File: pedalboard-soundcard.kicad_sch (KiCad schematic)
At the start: 21 parts, among them J1 RPi_GPIO, U1 AT24CS01-STUM, U2 NCP163, U3 NCP163, U5 NCP163

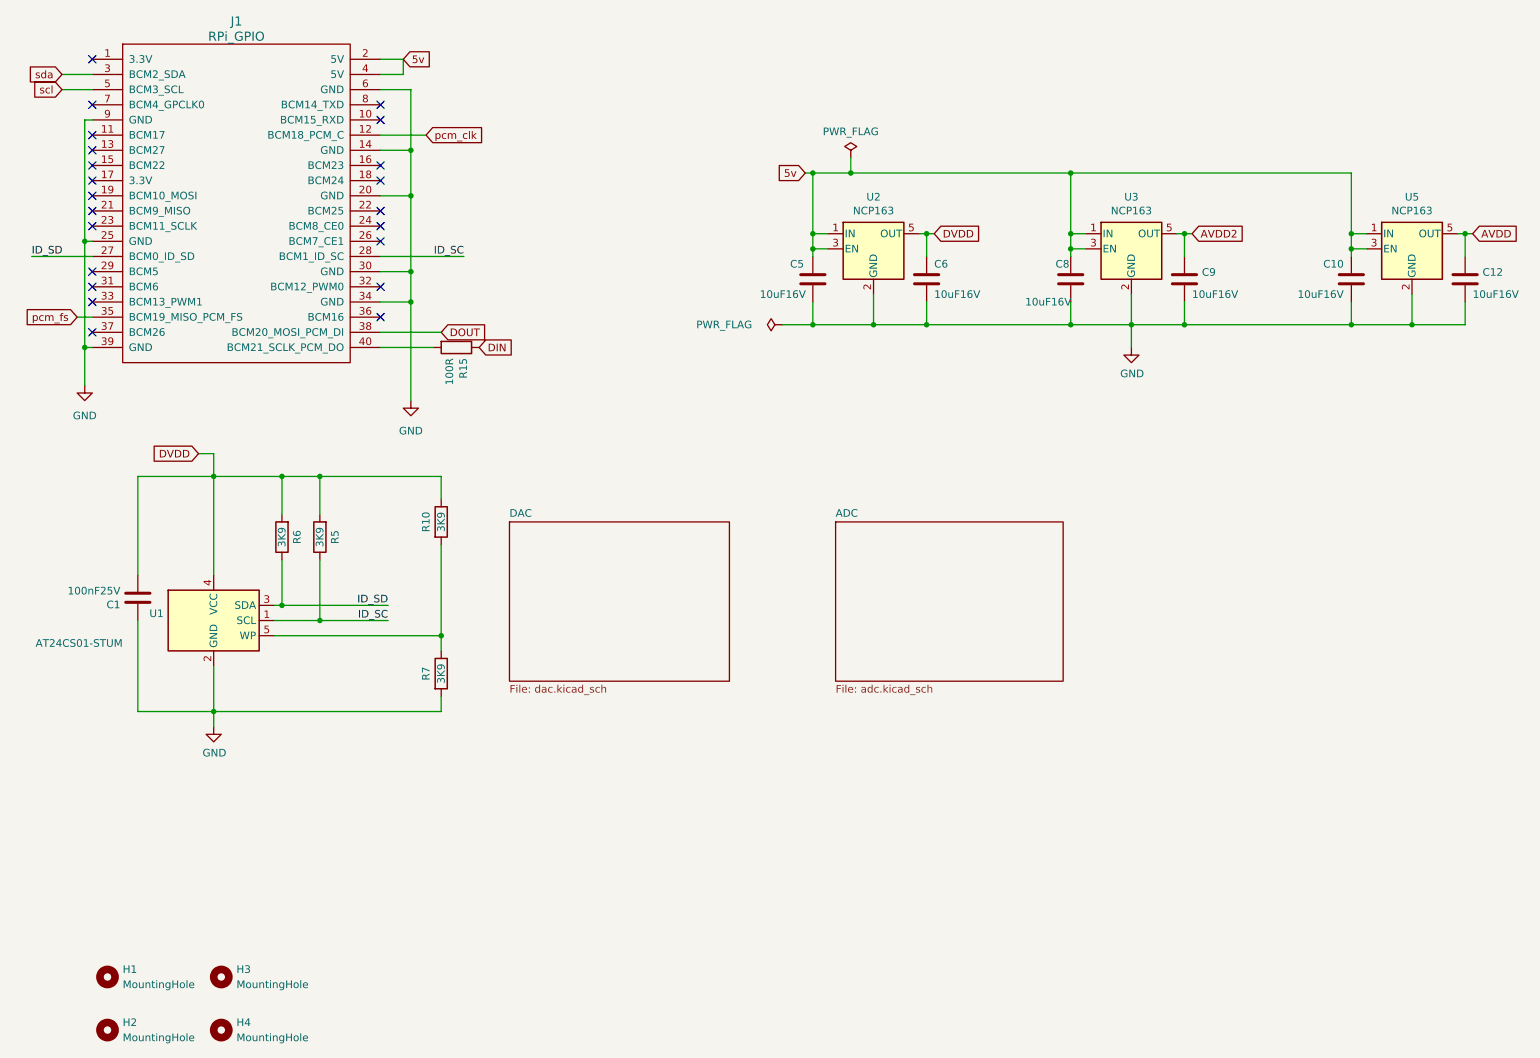
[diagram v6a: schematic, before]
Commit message: Replace 5v global label with +5V power
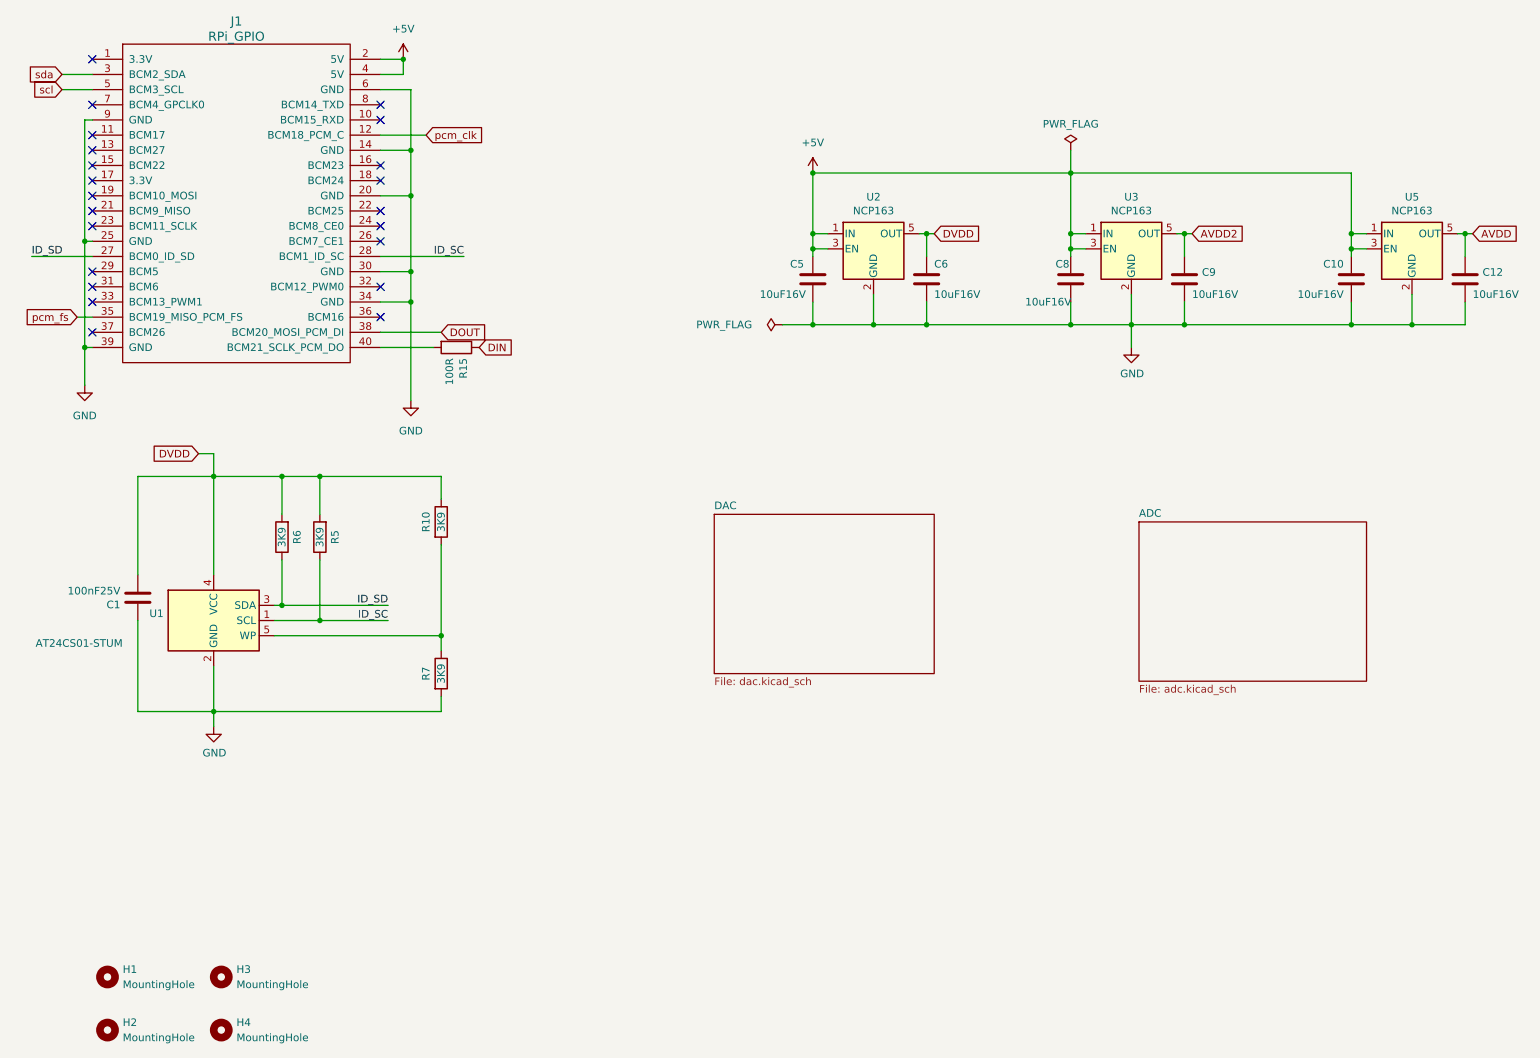
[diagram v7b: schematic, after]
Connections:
- net 5v renamed +5V
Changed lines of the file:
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@@
   (junction (at 44.45 96.52) (diameter 0) (color 0 0 0 0)
   )
+  (junction (at 144.78 45.72) (diameter 0) (color 0 0 0 0)
+  )
   (junction (at 234.95 71.12) (diameter 0) (color 0 0 0 0)
   )
   (junction (at 163.83 71.12) (diameter 0) (color 0 0 0 0)
   )
-  (junction (at 151.13 45.72) (diameter 0) (color 0 0 0 0)
-  )
   (junction (at 245.11 71.12) (diameter 0) (color 0 0 0 0)
   )
@@
   (junction (at 144.78 55.88) (diameter 0) (color 0 0 0 0)
   )
+  (junction (at 76.2 26.67) (diameter 0) (color 0 0 0 0)
+  )
   (junction (at 77.47 62.23) (diameter 0) (color 0 0 0 0)
   )
@@
   )
   (junction (at 77.47 49.53) (diameter 0) (color 0 0 0 0)
-  )
-  (junction (at 144.78 45.72) (diameter 0) (color 0 0 0 0)
   )
   (junction (at 77.47 41.91) (diameter 0) (color 0 0 0 0)
@@
     (stroke (width 0) (type default))
   )
-  (wire (pts (xy 143.51 45.72) (xy 144.78 45.72))
-    (stroke (width 0) (type default))
-  )
   (wire (pts (xy 207.01 55.88) (xy 208.28 55.88))
     (stroke (width 0) (type default))
@@
     (stroke (width 0) (type default))
   )
-  (wire (pts (xy 151.13 43.18) (xy 151.13 45.72))
+  (wire (pts (xy 187.96 41.91) (xy 187.96 45.72))
     (stroke (width 0) (type default))
   )
@@
     (stroke (width 0) (type default))
   )
-  (wire (pts (xy 144.78 45.72) (xy 151.13 45.72))
-    (stroke (width 0) (type default))
-  )
   (wire (pts (xy 31.75 96.52) (xy 31.75 113.03))
     (stroke (width 0) (type default))
@@
     (stroke (width 0) (type default))
   )
-  (wire (pts (xy 151.13 45.72) (xy 187.96 45.72))
+  (wire (pts (xy 144.78 45.72) (xy 187.96 45.72))
     (stroke (width 0) (type default))
   )
@@
     (effects (font (size 1.27 1.27)) (justify right))
     (property "Intersheetrefs" "${INTERSHEET_REFS}" (at 19.05 29.21 0)
-      (effects (font (size 1.27 1.27)) hide)
-    )
-  )
-  (global_label "5v" (shape input) (at 143.51 45.72 180)
-    (effects (font (size 1.27 1.27)) (justify right))
-    (property "Intersheetrefs" "${INTERSHEET_REFS}" (at 143.51 45.72 0)
       (effects (font (size 1.27 1.27)) hide)
     )
@@
     )
   )
-  (global_label "5v" (shape input) (at 76.2 26.67 0) (fields_autoplaced)
-    (effects (font (size 1.27 1.27)) (justify left))
-    (property "Intersheetrefs" "${INTERSHEET_REFS}" (at 80.7081 26.67 0)
-      (effects (font (size 1.27 1.27)) (justify left) hide)
-    )
-  )
   (global_label "DVDD" (shape input) (at 41.91 92.71 180)
     (effects (font (size 1.27 1.27)) (justify right))
@@
     )
   )
+  (symbol (lib_id "power:+5V") (at 76.2 26.67 0) (unit 1)
+    (in_bom yes) (on_board yes) (dnp no) (fields_autoplaced)
+    (property "Reference" "#PWR018" (at 76.2 30.48 0)
+      (effects (font (size 1.27 1.27)) hide)
+    )
+    (property "Value" "+5V" (at 76.2 21.59 0)
+      (effects (font (size 1.27 1.27)))
+    )
+    (property "Footprint" "" (at 76.2 26.67 0)
+      (effects (font (size 1.27 1.27)) hide)
+    )
+    (property "Datasheet" "" (at 76.2 26.67 0)
+      (effects (font (size 1.27 1.27)) hide)
+    )
+    (pin "1")
+    (instances
+      (project "pedalboard-soundcard"
+        (path "/257597c6-fbef-4478-b0f4-968f2d6f1866"
+          (reference "#PWR018") (unit 1)
+        )
+      )
+    )
+  )
+  (symbol (lib_id "power:+5V") (at 144.78 45.72 0) (unit 1)
+    (in_bom yes) (on_board yes) (dnp no) (fields_autoplaced)
+    (property "Reference" "#PWR019" (at 144.78 49.53 0)
+      (effects (font (size 1.27 1.27)) hide)
+    )
+    (property "Value" "+5V" (at 144.78 40.64 0)
+      (effects (font (size 1.27 1.27)))
+    )
+    (property "Footprint" "" (at 144.78 45.72 0)
+      (effects (font (size 1.27 1.27)) hide)
+    )
+    (property "Datasheet" "" (at 144.78 45.72 0)
+      (effects (font (size 1.27 1.27)) hide)
+    )
+    (pin "1")
+    (instances
+      (project "pedalboard-soundcard"
+        (path "/257597c6-fbef-4478-b0f4-968f2d6f1866"
+          (reference "#PWR019") (unit 1)
+        )
+      )
+    )
+  )
   (symbol (lib_id "Device:C") (at 234.95 63.5 0) (mirror y) (unit 1)
     (in_bom yes) (on_board yes) (dnp no)
@@
     )
   )
-  (symbol (lib_id "power:PWR_FLAG") (at 151.13 43.18 0) (unit 1)
-    (in_bom yes) (on_board yes) (dnp no)
-    (property "Reference" "#FLG02" (at 151.13 41.275 0)
-      (effects (font (size 1.27 1.27)) hide)
-    )
-    (property "Value" "PWR_FLAG" (at 151.13 38.7858 0)
-      (effects (font (size 1.27 1.27)))
-    )
-    (property "Footprint" "" (at 151.13 43.18 0)
-      (effects (font (size 1.27 1.27)) hide)
-    )
-    (property "Datasheet" "~" (at 151.13 43.18 0)
+  (symbol (lib_id "power:PWR_FLAG") (at 187.96 41.91 0) (unit 1)
+    (in_bom yes) (on_board yes) (dnp no)
+    (property "Reference" "#FLG02" (at 187.96 40.005 0)
+      (effects (font (size 1.27 1.27)) hide)
+    )
+    (property "Value" "PWR_FLAG" (at 187.96 37.5158 0)
+      (effects (font (size 1.27 1.27)))
+    )
+    (property "Footprint" "" (at 187.96 41.91 0)
+      (effects (font (size 1.27 1.27)) hide)
+    )
+    (property "Datasheet" "~" (at 187.96 41.91 0)
       (effects (font (size 1.27 1.27)) hide)
     )
@@
     )
   )
-  (sheet (at 148.59 104.14) (size 38.1 26.67) (fields_autoplaced)
+  (sheet (at 199.39 104.14) (size 38.1 26.67) (fields_autoplaced)
     (stroke (width 0.1524) (type solid))
     (fill (color 0 0 0 0.0000))
-    (property "Sheetname" "ADC" (at 148.59 103.4284 0)
+    (property "Sheetname" "ADC" (at 199.39 103.4284 0)
       (effects (font (size 1.27 1.27)) (justify left bottom))
     )
-    (property "Sheetfile" "adc.kicad_sch" (at 148.59 131.3946 0)
+    (property "Sheetfile" "adc.kicad_sch" (at 199.39 131.3946 0)
       (effects (font (size 1.27 1.27)) (justify left top))
     )
@@
     )
   )
-  (sheet (at 93.98 104.14) (size 36.83 26.67) (fields_autoplaced)
+  (sheet (at 128.27 102.87) (size 36.83 26.67) (fields_autoplaced)
     (stroke (width 0.1524) (type solid))
     (fill (color 0 0 0 0.0000))
-    (property "Sheetname" "DAC" (at 93.98 103.4284 0)
+    (property "Sheetname" "DAC" (at 128.27 102.1584 0)
       (effects (font (size 1.27 1.27)) (justify left bottom))
     )
-    (property "Sheetfile" "dac.kicad_sch" (at 93.98 131.3946 0)
+    (property "Sheetfile" "dac.kicad_sch" (at 128.27 130.1246 0)
       (effects (font (size 1.27 1.27)) (justify left top))
     )

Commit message: Replace DVDD global label with VDD power symbol
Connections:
- net DVDD renamed VDD
